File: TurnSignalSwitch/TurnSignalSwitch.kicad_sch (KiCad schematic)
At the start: 1 part, among them J0 C-

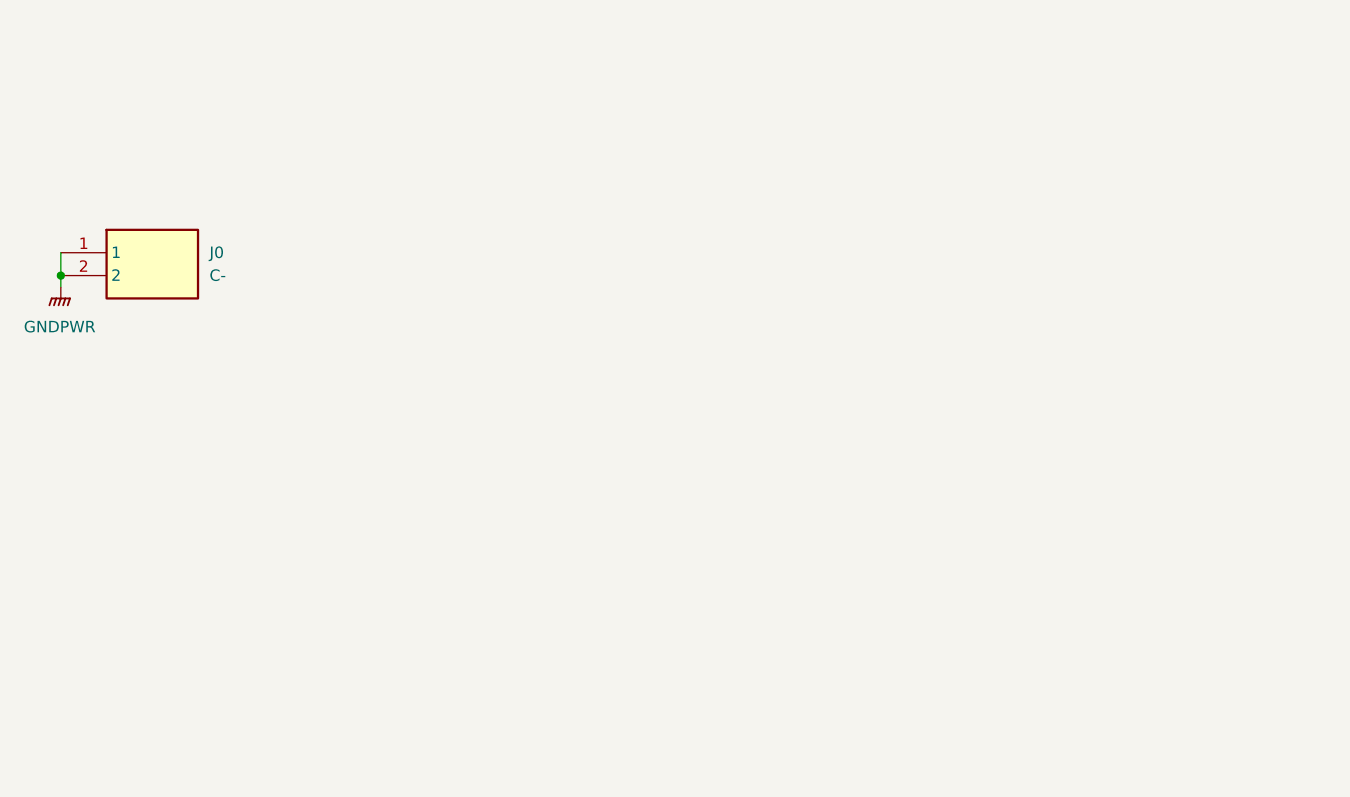
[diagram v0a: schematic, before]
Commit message: Completed control boards.
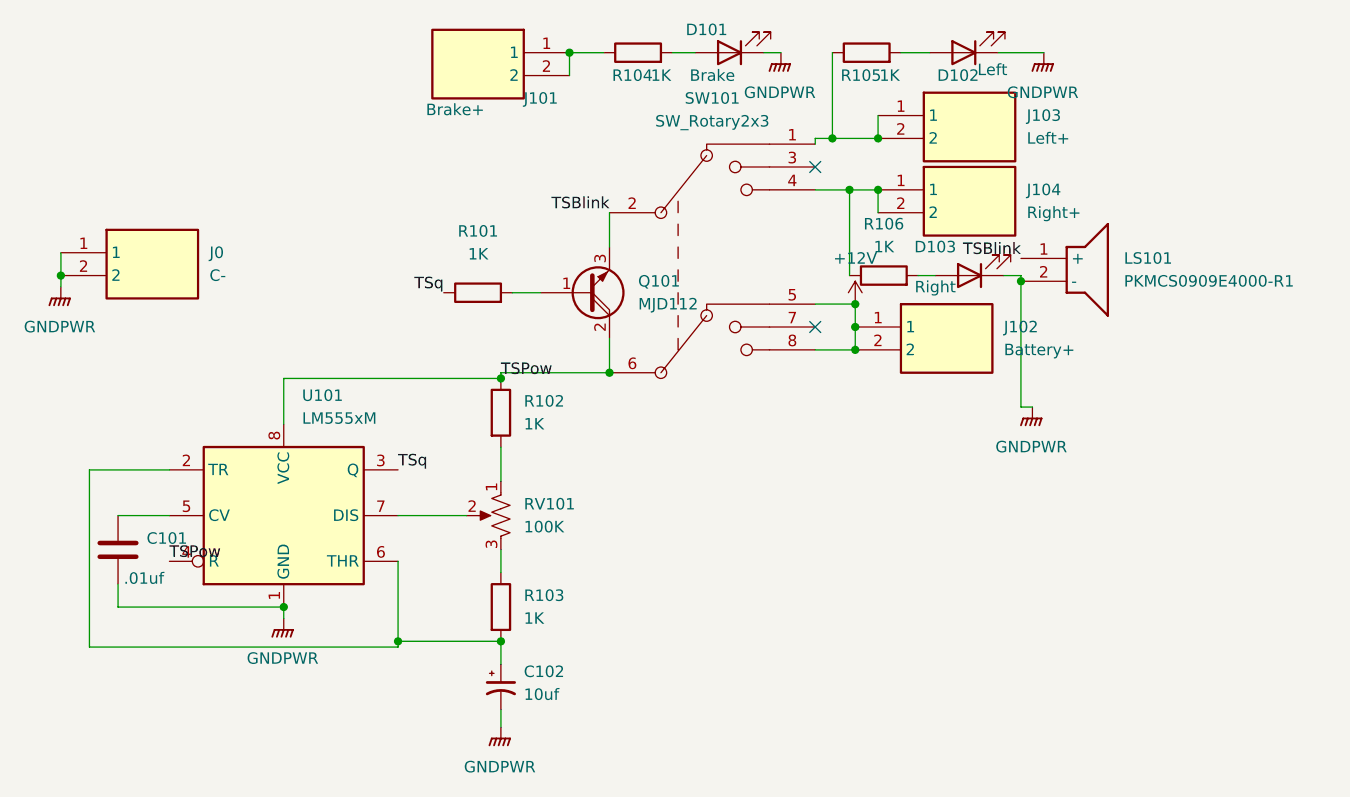
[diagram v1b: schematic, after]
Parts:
- added C101: .01uf, Capacitor_SMD:C_0402_1005Metric, symbol Device:C
- added C102: 10uf, Capacitor_SMD:C_1206_3216Metric, symbol Device:C_Polarized_Small_US
- added D101: Brake, LED_SMD:LED_0603_1608Metric, symbol Device:LED
- added D102: Left, LED_SMD:LED_0603_1608Metric, symbol Device:LED
- added D103: Right, LED_SMD:LED_0603_1608Metric, symbol Device:LED
- added J101: Brake+, SpadeLugs:197054303, symbol SpadeLugs:19705-4303
- added J102: Battery+, SpadeLugs:197054303, symbol SpadeLugs:19705-4303
- added J103: Left+, SpadeLugs:197054303, symbol SpadeLugs:19705-4303
- added J104: Right+, SpadeLugs:197054303, symbol SpadeLugs:19705-4303
- added LS101: PKMCS0909E4000-R1, Piezo:PKMCS0909E4000R1, symbol Piezo:PKMCS0909E4000-R1
- added Q101: MJD112, Package_TO_SOT_SMD:TO-252-2, symbol Device:Q_NPN_Darlington_BCE
- added R101, R102, R103, R104, R105, R106: 1K, Resistor_SMD:R_0603_1608Metric, symbol Device:R
- added RV101: 100K, BournsPVG3A:PVG3A103C01R00, symbol Device:R_Potentiometer_US
- added SW101: SW_Rotary2x3, Package_DIP:DIP-8_W7.62mm, symbol SS-10:SW_Rotary2x3
- added U101: LM555xM, Package_SO:SOIC-8_3.9x4.9mm_P1.27mm, symbol Timer:LM555xM
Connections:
- net GNDPWR: now also C101.2, C102.2, D101.1 (K), D102.1 (K), D103.1 (K), LS101.2 (-), U101.1 (GND)
- new net: Q101.1 (B), R101.2
- new net: J101.1, J101.2, R104.1
- new net: D101.2 (A), R104.2
- new net: R103.1, RV101.3
- new net: C102.1, R103.2, U101.2 (TR), U101.6 (THR)
- new net: J103.1, J103.2, R105.1, SW101.1 (1-1)
- new net: J104.1, J104.2, R106.1, SW101.4 (1-3)
- new net: R102.2, RV101.1
- new net: RV101.2, U101.7 (DIS)
- new net: C101.1, U101.5 (CV)
- new net: D103.2 (A), R106.2
- new net: D102.2 (A), R105.2
- new net +12V: J102.1, J102.2, SW101.5 (2-1), SW101.8 (2-3)
- new net TSBlink: LS101.1 (+), Q101.3 (E), SW101.2 (C1)
- new net TSPow: Q101.2 (C), R102.1, SW101.6 (C2), U101.4 (R), U101.8 (VCC)
- new net TSq: R101.1, U101.3 (Q)
- no-connect marks 0 -> 2
